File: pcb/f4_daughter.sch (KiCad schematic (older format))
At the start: 0 parts

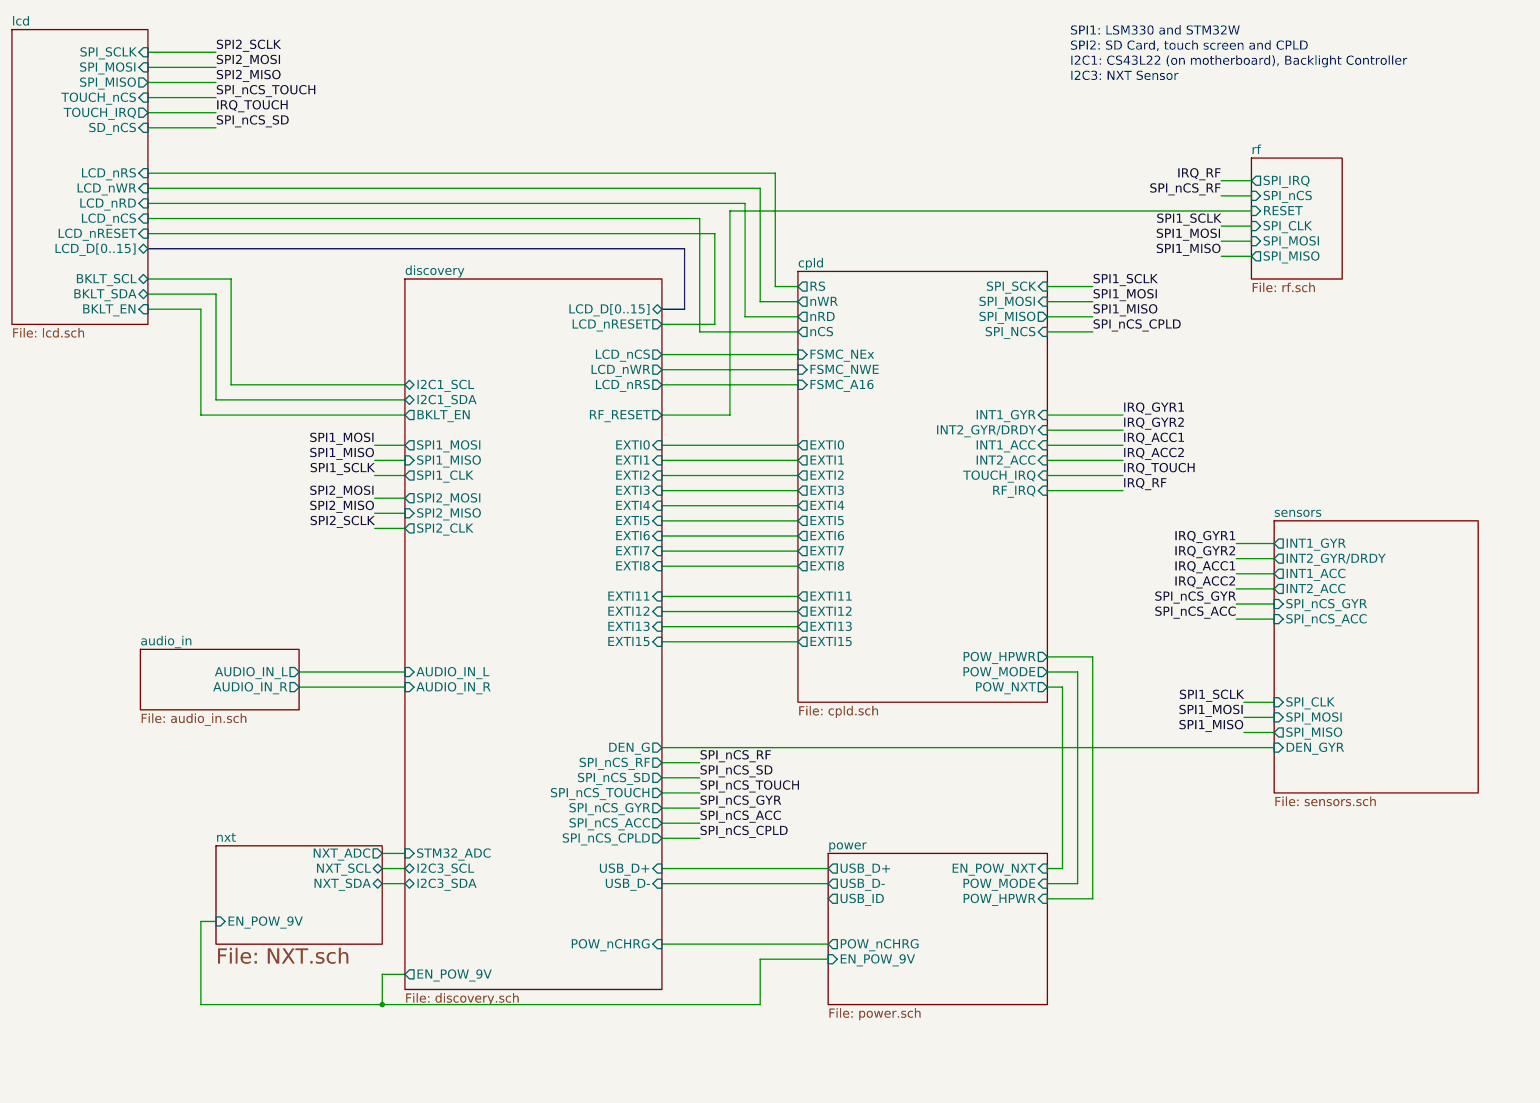
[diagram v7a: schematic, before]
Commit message: Fixed a few things: CPLD_EN now a pin on STM32F4 Took FSMC_A16 off of CPLD Put BKLT_EN on the CPLD Rework FTDI chip connections
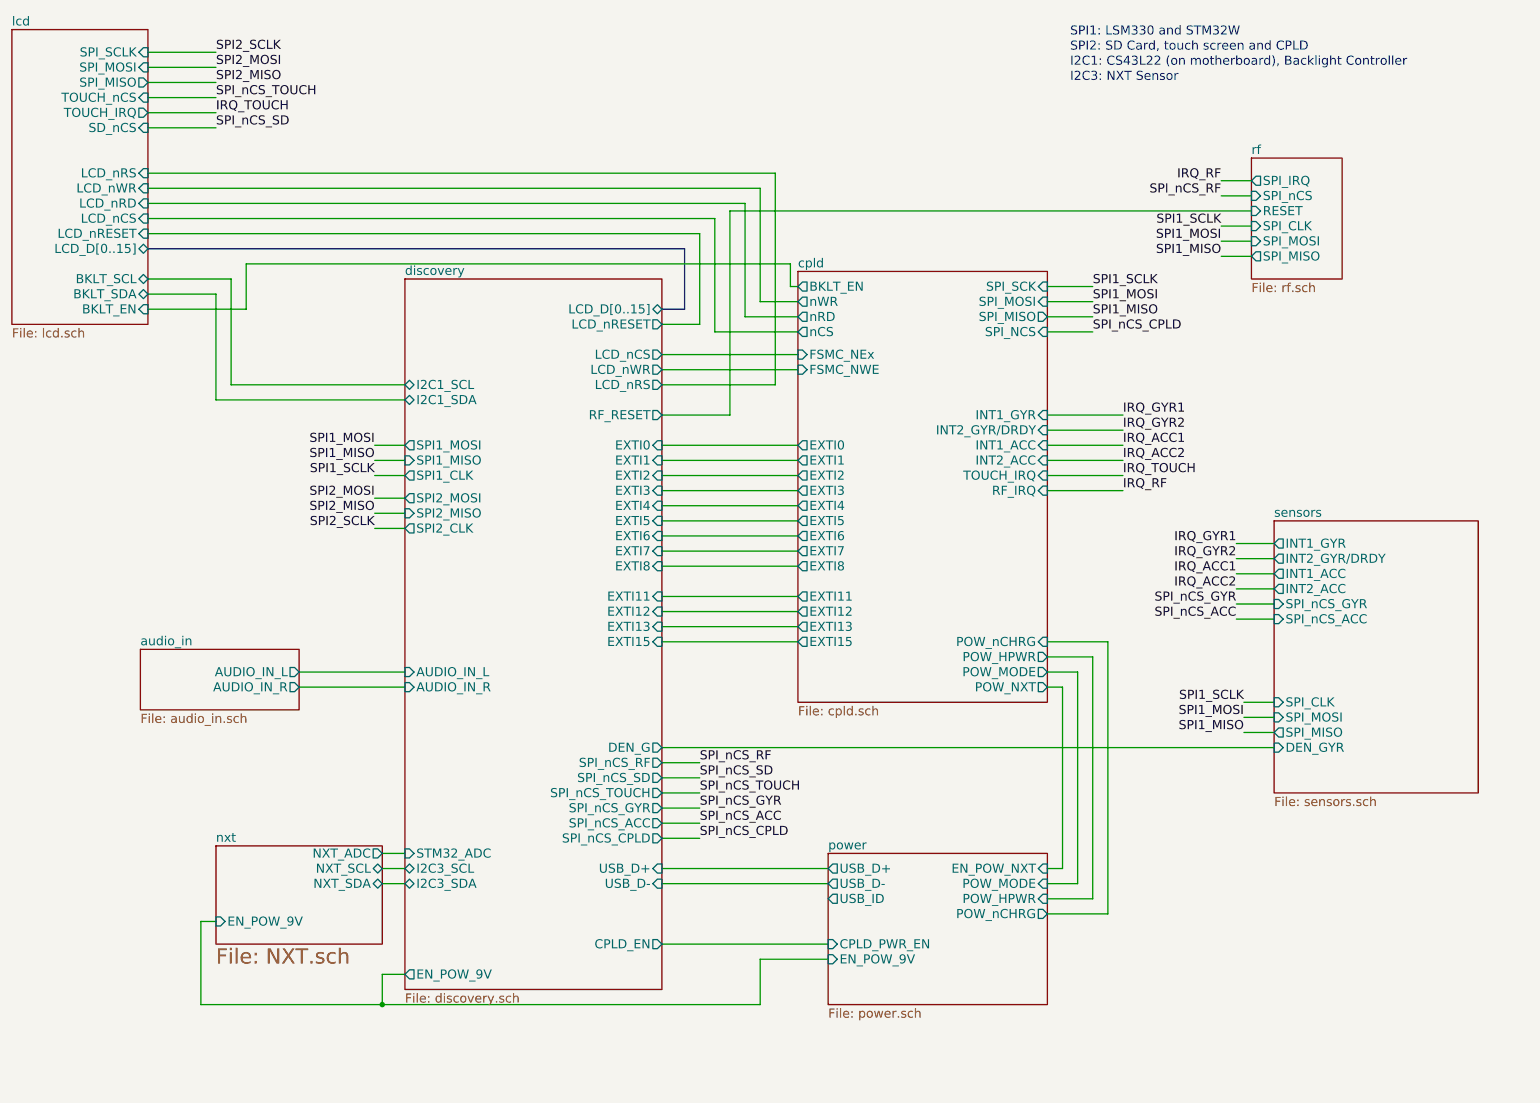
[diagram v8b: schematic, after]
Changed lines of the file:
@@
-EESchema Schematic File Version 2  date Wed 16 Jan 2013 06:45:33 PM EST
+EESchema Schematic File Version 2  date Thu 17 Jan 2013 02:12:00 PM EST
 LIBS:power
 LIBS:device
@@
 Sheet 1 9
 Title ""
-Date "16 jan 2013"
+Date "17 jan 2013"
 Rev ""
 Comp ""
@@
 $EndDescr
 Wire Wire Line
-	5650 6700 6750 6700
+	8200 6500 8600 6500
+Wire Wire Line
+	8600 6500 8600 4700
+Wire Wire Line
+	8600 4700 8200 4700
+Wire Wire Line
+	2250 2500 2900 2500
+Wire Wire Line
+	2900 2500 2900 2200
+Wire Wire Line
+	2900 2200 6500 2200
+Wire Wire Line
+	6500 2200 6500 2350
+Wire Wire Line
+	6500 2350 6550 2350
 Wire Wire Line
 	8200 4800 8500 4800
@@
 	2250 1600 6400 1600
 Wire Wire Line
-	6400 1600 6400 2350
-Wire Wire Line
-	6400 2350 6550 2350
-Wire Wire Line
 	8700 3300 8200 3300
 Wire Wire Line
@@
 	5650 2900 6550 2900
 Wire Wire Line
-	5650 2600 6000 2600
+	5650 2600 5900 2600
 Wire Wire Line
 	9700 4550 9450 4550
@@
 	2700 900  2250 900
 Wire Wire Line
-	2250 2000 6000 2000
-Wire Wire Line
-	6000 2000 6000 2600
+	2250 2000 5900 2000
+Wire Wire Line
+	5900 2000 5900 2600
 Wire Bus Line
 	2250 2100 5800 2100
@@
 	5650 3200 6100 3200
 Wire Wire Line
-	5650 3000 6550 3000
-Wire Wire Line
 	5650 3500 6550 3500
 Wire Wire Line
@@
 	6300 1700 2250 1700
 Wire Wire Line
-	6550 2650 5900 2650
-Wire Wire Line
-	5900 2650 5900 1900
-Wire Wire Line
-	5900 1900 2250 1900
+	6550 2650 6000 2650
+Wire Wire Line
+	6000 2650 6000 1900
+Wire Wire Line
+	6000 1900 2250 1900
 Wire Wire Line
 	8700 3700 8200 3700
@@
 Wire Wire Line
 	2800 2300 2250 2300
-Wire Wire Line
-	3950 3200 2600 3200
-Wire Wire Line
-	2600 3200 2600 2500
-Wire Wire Line
-	2600 2500 2250 2500
 Wire Wire Line
 	6750 6300 5650 6300
@@
 	3800 6900 3800 7100
 Connection ~ 3800 7100
+Wire Wire Line
+	5650 3000 6400 3000
+Wire Wire Line
+	6400 3000 6400 1600
+Wire Wire Line
+	6750 6700 5650 6700
+$Sheet
+S 6750 6100 1450 1000
+U 500B69F1
+F0 "power" 60
+F1 "power.sch" 60
+F2 "USB_ID" O L 6750 6400 60
+F3 "USB_D+" O L 6750 6200 60
+F4 "USB_D-" O L 6750 6300 60
+F5 "POW_MODE" I R 8200 6300 60
+F6 "POW_nCHRG" O R 8200 6500 60
+F7 "POW_HPWR" I R 8200 6400 60
+F8 "EN_POW_NXT" I R 8200 6200 60
+F9 "EN_POW_9V" I L 6750 6800 60
+F10 "CPLD_PWR_EN" I L 6750 6700 60
+$EndSheet
 $Sheet
 S 9700 3900 1350 1800
@@
 F40 "EXTI15" I R 5650 4700 60
 F41 "EXTI12" I R 5650 4500 60
-F42 "BKLT_EN" O L 3950 3200 60
-F43 "I2C1_SCL" B L 3950 3000 60
-F44 "I2C1_SDA" B L 3950 3100 60
-F45 "POW_nCHRG" I R 5650 6700 60
+F42 "I2C1_SCL" B L 3950 3000 60
+F43 "I2C1_SDA" B L 3950 3100 60
+F44 "CPLD_EN" O R 5650 6700 60
 $EndSheet
 Text Label 8500 2650 0    60   ~ 0
@@
 F3 "POW_NXT" O R 8200 5000 60
 F4 "POW_MODE" O R 8200 4900 60
-F5 "FSMC_A16" I L 6550 3000 60
-F6 "FSMC_NWE" I L 6550 2900 60
-F7 "FSMC_NEx" I L 6550 2800 60
-F8 "EXTI0" O L 6550 3400 60
-F9 "EXTI1" O L 6550 3500 60
-F10 "EXTI2" O L 6550 3600 60
-F11 "EXTI3" O L 6550 3700 60
-F12 "EXTI4" O L 6550 3800 60
-F13 "EXTI5" O L 6550 3900 60
-F14 "EXTI8" O L 6550 4200 60
-F15 "EXTI7" O L 6550 4100 60
-F16 "EXTI6" O L 6550 4000 60
-F17 "SPI_MISO" O R 8200 2550 60
-F18 "SPI_NCS" I R 8200 2650 60
-F19 "SPI_MOSI" I R 8200 2450 60
-F20 "SPI_SCK" I R 8200 2350 60
-F21 "RS" O L 6550 2350 60
-F22 "nWR" O L 6550 2450 60
-F23 "nRD" O L 6550 2550 60
-F24 "nCS" O L 6550 2650 60
-F25 "TOUCH_IRQ" I R 8200 3600 60
-F26 "RF_IRQ" I R 8200 3700 60
-F27 "INT2_GYR/DRDY" I R 8200 3300 60
-F28 "INT1_GYR" I R 8200 3200 60
-F29 "INT2_ACC" I R 8200 3500 60
-F30 "INT1_ACC" I R 8200 3400 60
-F31 "EXTI11" O L 6550 4400 60
-F32 "EXTI13" O L 6550 4600 60
-F33 "EXTI15" O L 6550 4700 60
-F34 "EXTI12" O L 6550 4500 60
+F5 "FSMC_NWE" I L 6550 2900 60
+F6 "FSMC_NEx" I L 6550 2800 60
+F7 "EXTI0" O L 6550 3400 60
+F8 "EXTI1" O L 6550 3500 60
+F9 "EXTI2" O L 6550 3600 60
+F10 "EXTI3" O L 6550 3700 60
+F11 "EXTI4" O L 6550 3800 60
+F12 "EXTI5" O L 6550 3900 60
+F13 "EXTI8" O L 6550 4200 60
+F14 "EXTI7" O L 6550 4100 60
+F15 "EXTI6" O L 6550 4000 60
+F16 "SPI_MISO" O R 8200 2550 60
+F17 "SPI_NCS" I R 8200 2650 60
+F18 "SPI_MOSI" I R 8200 2450 60
+F19 "SPI_SCK" I R 8200 2350 60
+F20 "nWR" O L 6550 2450 60
+F21 "nRD" O L 6550 2550 60
+F22 "nCS" O L 6550 2650 60
+F23 "TOUCH_IRQ" I R 8200 3600 60
+F24 "RF_IRQ" I R 8200 3700 60
+F25 "INT2_GYR/DRDY" I R 8200 3300 60
+F26 "INT1_GYR" I R 8200 3200 60
+F27 "INT2_ACC" I R 8200 3500 60
+F28 "INT1_ACC" I R 8200 3400 60
+F29 "EXTI11" O L 6550 4400 60
+F30 "EXTI13" O L 6550 4600 60
+F31 "EXTI15" O L 6550 4700 60
+F32 "EXTI12" O L 6550 4500 60
+F33 "BKLT_EN" O L 6550 2350 60
+F34 "POW_nCHRG" I R 8200 4700 60
 $EndSheet
 Text Label 5900 5500 0    60   ~ 0
@@
 $EndSheet
 $Sheet
-S 6750 6100 1450 1000
-U 500B69F1
-F0 "power" 60
-F1 "power.sch" 60
-F2 "USB_ID" O L 6750 6400 60
-F3 "USB_D+" O L 6750 6200 60
-F4 "USB_D-" O L 6750 6300 60
-F5 "POW_MODE" I R 8200 6300 60
-F6 "POW_nCHRG" O L 6750 6700 60
-F7 "POW_HPWR" I R 8200 6400 60
-F8 "EN_POW_NXT" I R 8200 6200 60
-F9 "EN_POW_9V" I L 6750 6800 60
-$EndSheet
-$Sheet
